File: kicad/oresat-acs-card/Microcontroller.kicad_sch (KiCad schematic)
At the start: 23 parts, among them J2 ORESAT-DEBUG-CONNECTOR-SOLAR, U14 TCAN330GDCNT, U15 STM32F042K6T7, X2 ECS-160-10-36Q-ES-TR

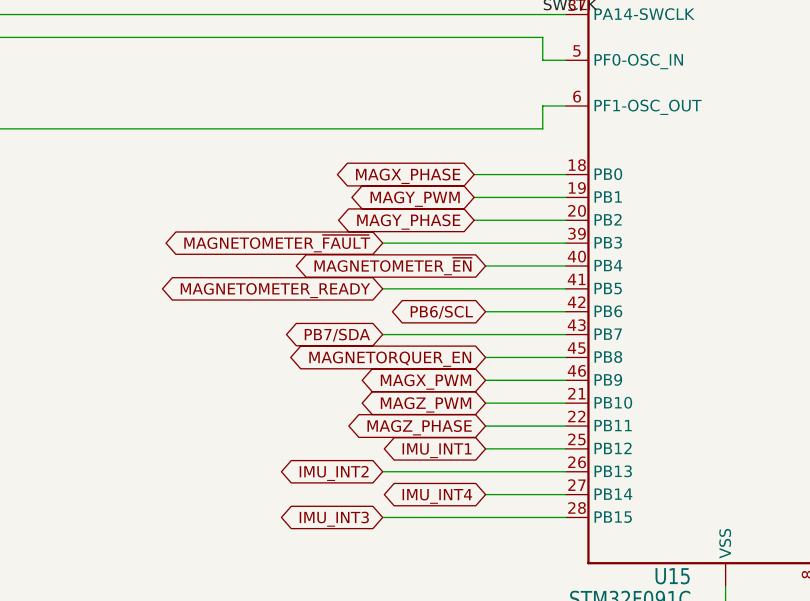
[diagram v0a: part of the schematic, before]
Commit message: Updated PCB layoud. Changed magnetorquer connection to 6 position pin terminal
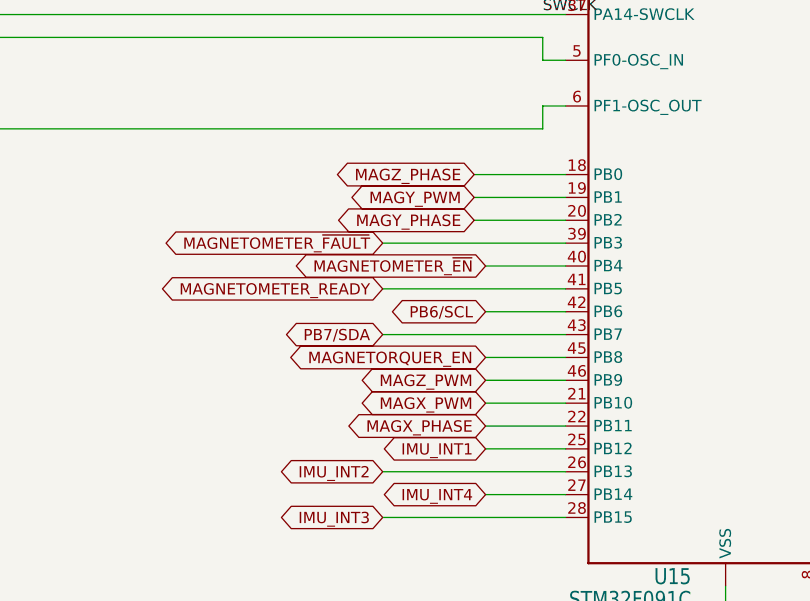
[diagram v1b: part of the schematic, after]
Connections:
- net MAGX_PHASE: now also U15.22 (PB11); no longer U15.18 (PB0)
- net MAGX_PWM: now also U15.21 (PB10); no longer U15.46 (PB9)
- net MAGZ_PHASE: now also U15.18 (PB0); no longer U15.22 (PB11)
- net MAGZ_PWM: now also U15.46 (PB9); no longer U15.21 (PB10)
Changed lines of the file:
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@@
     (effects (font (size 1.2446 1.2446)) (justify left bottom))
   )
-  (global_label "MAGZ_PWM" (shape bidirectional) (at 204.47 137.16 180) (fields_autoplaced)
+  (global_label "MAGX_PWM" (shape bidirectional) (at 204.47 137.16 180) (fields_autoplaced)
     (effects (font (size 1.27 1.27)) (justify right))
     (property "Intersheet References" "${INTERSHEET_REFS}" (id 0) (at 191.8969 137.0806 0)
@@
     )
   )
-  (global_label "MAGZ_PHASE" (shape bidirectional) (at 204.47 139.7 180) (fields_autoplaced)
+  (global_label "MAGX_PHASE" (shape bidirectional) (at 204.47 139.7 180) (fields_autoplaced)
     (effects (font (size 1.27 1.27)) (justify right))
     (property "Intersheet References" "${INTERSHEET_REFS}" (id 0) (at 190.0221 139.6206 0)
@@
     )
   )
-  (global_label "MAGX_PWM" (shape bidirectional) (at 204.47 134.62 180) (fields_autoplaced)
+  (global_label "MAGZ_PWM" (shape bidirectional) (at 204.47 134.62 180) (fields_autoplaced)
     (effects (font (size 1.27 1.27)) (justify right))
     (property "Intersheet References" "${INTERSHEET_REFS}" (id 0) (at 191.8969 134.5406 0)
@@
     )
   )
-  (global_label "MAGX_PHASE" (shape bidirectional) (at 203.2 111.76 180) (fields_autoplaced)
+  (global_label "MAGZ_PHASE" (shape bidirectional) (at 203.2 111.76 180) (fields_autoplaced)
     (effects (font (size 1.27 1.27)) (justify right))
     (property "Intersheet References" "${INTERSHEET_REFS}" (id 0) (at 188.7521 111.6806 0)

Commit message: Updated 5 V regulator and tweaked card layout. Cleaned up silkscreen layer and schematic.
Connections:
- net PB6/SCL: no longer R11.1
- net PB7/SDA: no longer R12.1
- net MAGNETOMETER_READY renamed MAG_READY
- net MAGNETOMETER_~{EN} renamed MAG_~{EN}
- net MAGNETOMETER_~{FAULT} renamed MAG_~{FAULT}
- net MAGNETORQUER_EN renamed MT_EN
- net MAGNETORQUER_FAULT renamed MT_FAULT
- net MAGNETORQUER_ILIM renamed MT_ILIM
- net MAGNETORQUER_STBY/RST renamed MT_STBY/RST
- net MAGX_ISENSE renamed MT_X_ISENSE
- net MAGX_PHASE renamed MT_X_PHASE
- net MAGX_PWM renamed MT_X_PWM
- net MAGY_ISENSE renamed MT_Y_ISENSE
- net MAGY_PHASE renamed MT_Y_PHASE
- net MAGY_PWM renamed MT_Y_PWM
- net MAGZ_ISENSE renamed MT_Z_ISENSE
- net MAGZ_PHASE renamed MT_Z_PHASE
- net MAGZ_PWM renamed MT_Z_PWM
- net PA8/POUTPROT renamed PA8/POUTPROT
- net PA9/CAN_SILENT renamed PA9/CAN_SILENT
- new net PB6/SCL: R11.1
- new net PB7/SDA: R12.1
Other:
- note added: "Note: MT = Magnetorquer MAG = Magnetometer"
- moved on the sheet: C28, C29, C30, C36, C37, C38, C39, D2, J2, R11, R12, R7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

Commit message: Design review changes.
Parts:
- J2: footprint oresat-acs-card:WURTH_687120183622 -> oresat-footprints:J-TE_2-1734592-0; symbol oresat-acs-card-eagle-import:ORESAT-DEBUG-CONNECTOR-SOLAR -> J-TE-2-1734592-0-oresat-debug-connector:J-TE-Debug-2-1734592-0
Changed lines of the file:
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@@
     (pin "1")
   )
-  (symbol (lib_id "oresat-acs-card-eagle-import:ORESAT-DEBUG-CONNECTOR-SOLAR") (at 27.94 198.12 0) (unit 1)
+  (symbol (lib_id "J-TE-2-1734592-0-oresat-debug-connector:J-TE-Debug-2-1734592-0") (at 29.21 198.12 0) (unit 1)
     (in_bom yes) (on_board yes)
-    (property "Reference" "J2" (id 0) (at 25.4 166.37 0)
+    (property "Reference" "J2" (id 0) (at 26.67 166.37 0)
       (effects (font (size 2.0828 1.7703)) (justify left bottom))
     )
-    (property "Value" "ORESAT-DEBUG-CONNECTOR-SOLAR" (id 1) (at 27.94 198.12 0)
+    (property "Value" "ORESAT-DEBUG-CONNECTOR-SOLAR" (id 1) (at 29.21 198.12 0)
       (effects (font (size 1.27 1.27)) hide)
     )
-    (property "Footprint" "oresat-acs-card:WURTH_687120183622" (id 2) (at 27.94 198.12 0)
+    (property "Footprint" "oresat-footprints:J-TE_2-1734592-0" (id 2) (at 29.21 189.23 0)
       (effects (font (size 1.27 1.27)) hide)
     )
-    (property "Datasheet" "" (id 3) (at 27.94 198.12 0)
+    (property "Datasheet" "" (id 3) (at 29.21 189.23 0)
       (effects (font (size 1.27 1.27)) hide)
     )

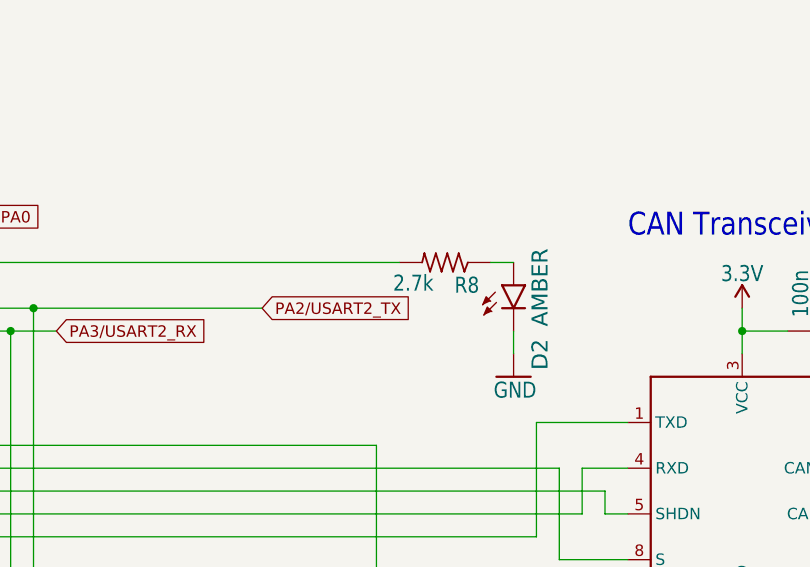
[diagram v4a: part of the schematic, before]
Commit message: Updated some attributes and resistor values to clean up BOM
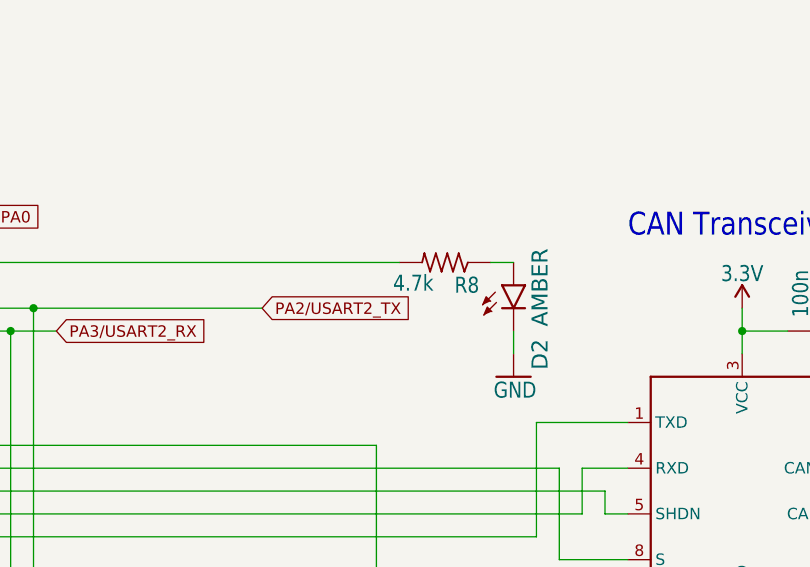
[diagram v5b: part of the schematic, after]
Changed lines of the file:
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@@
       (effects (font (size 1.778 1.5113)) (justify left bottom))
     )
-    (property "Value" "2.7k" (id 1) (at 334.01 85.09 0)
+    (property "Value" "4.7k" (id 1) (at 334.01 85.09 0)
       (effects (font (size 1.778 1.5113)) (justify left bottom))
     )
